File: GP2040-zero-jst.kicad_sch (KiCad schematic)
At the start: 12 parts, among them J1 Conn_01x04_Socket, K1 Conn_01x02_Socket, K2 Conn_01x02_Socket, K3 Conn_01x02_Socket, K4 Conn_01x02_Socket, P1 Conn_01x02_Socket, P2 Conn_01x02_Socket, P3 Conn_01x02_Socket, P4 Conn_01x02_Socket

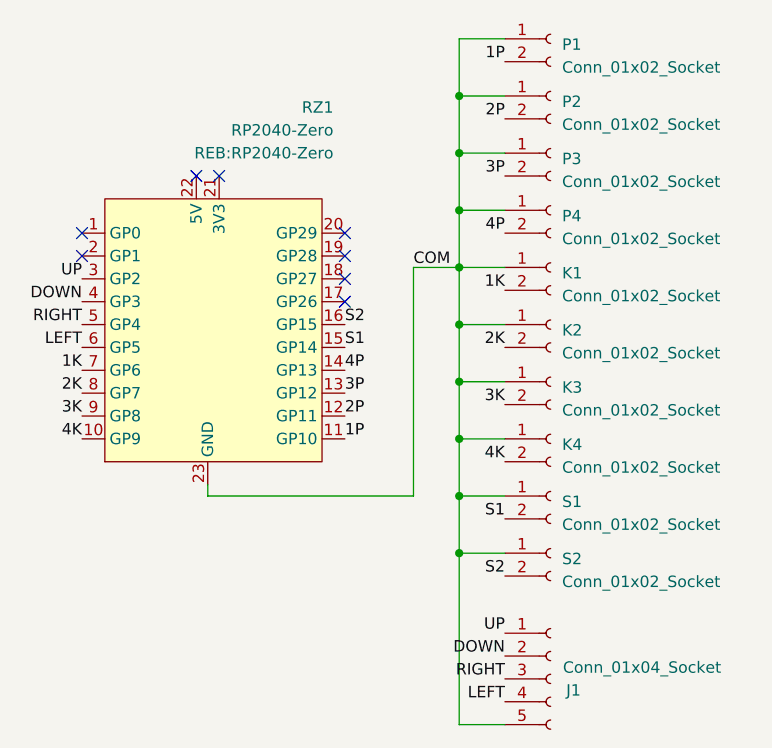
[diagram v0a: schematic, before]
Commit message: Widen mounting holes, rewire for no-config
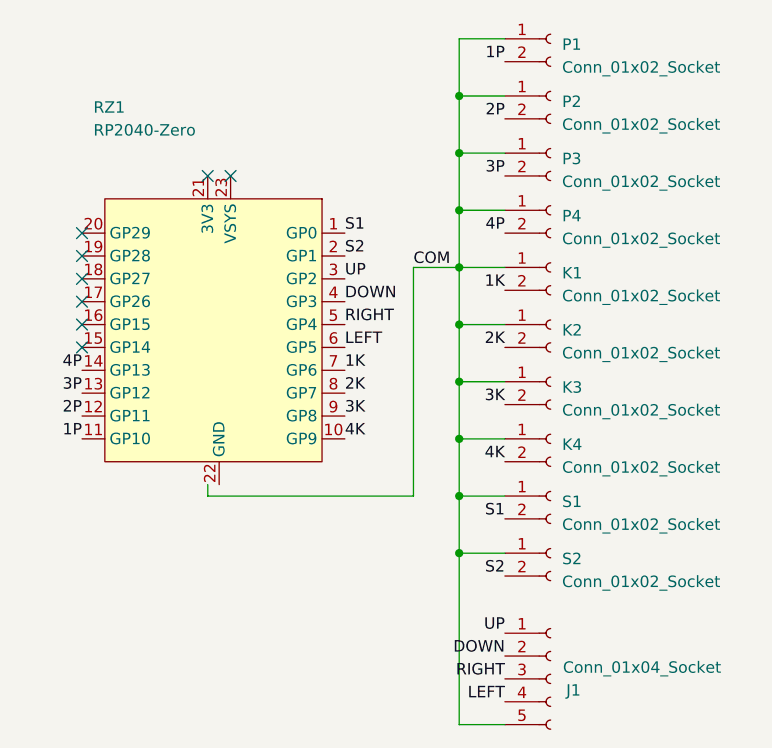
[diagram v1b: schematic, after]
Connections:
- net COM: no longer RZ1.23 (GND)
- net S1: now also RZ1.1 (GP0); no longer RZ1.15 (GP14)
- net S2: now also RZ1.2 (GP1); no longer RZ1.16 (GP15)
